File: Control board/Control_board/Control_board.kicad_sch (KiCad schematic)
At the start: 56 parts, among them J1 KEYPAD, J2 UART_conn, J3 Power_IN, J4 SPI_conn, SW1 RESET, U1 AT45DB321E-SHF-T, U10 SP3485EN, U2 LM2576HVS-5, U3 LoRa, U4 Wifi, U5 LM1117LD-3.3, U6 STM32F103C8Tx, U7 RTC_DS3234, U8 DS3232SN-T&R, U9 OLED, Y1 8MHZ

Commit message: edit layout
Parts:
- added D7: DF02S, Diode_SMD:Diode_Bridge_OnSemi_SDIP-4L, symbol Diode_Bridge:DF02S
- TH1, TH2: value Thermistor_PTC -> 250-120U
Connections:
- net 12V: now also D7.1 (+); no longer J3.1 (Pin_1)
- net GND: now also D7.2 (-); no longer J3.2 (Pin_2)
- new net: D7.3, J3.2 (Pin_2)
- new net: D7.4, J3.1 (Pin_1)
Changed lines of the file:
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@@
 	(wire
 		(pts
+			(xy 226.06 132.715) (xy 226.06 125.73)
+		)
+		(stroke
+			(width 0)
+			(type default)
+		)
+	)
+	(wire
+		(pts
 			(xy 205.105 29.21) (xy 205.105 34.29)
 		)
@@
 	(wire
 		(pts
-			(xy 234.95 135.255) (xy 240.03 135.255)
+			(xy 68.58 36.83) (xy 71.755 36.83)
 		)
 		(stroke
@@
 	(wire
 		(pts
-			(xy 68.58 36.83) (xy 71.755 36.83)
+			(xy 78.74 106.68) (xy 85.725 106.68)
 		)
 		(stroke
@@
 	(wire
 		(pts
-			(xy 78.74 106.68) (xy 85.725 106.68)
+			(xy 123.19 73.66) (xy 130.81 73.66)
 		)
 		(stroke
@@
 	(wire
 		(pts
-			(xy 123.19 73.66) (xy 130.81 73.66)
+			(xy 212.09 125.73) (xy 212.09 128.905)
 		)
 		(stroke
@@
 	(wire
 		(pts
+			(xy 226.06 135.255) (xy 226.06 144.145)
+		)
+		(stroke
+			(width 0)
+			(type default)
+		)
+	)
+	(wire
+		(pts
 			(xy 67.31 160.655) (xy 75.565 160.655)
 		)
@@
 	(wire
 		(pts
-			(xy 55.88 44.45) (xy 55.88 41.91)
+			(xy 219.71 136.525) (xy 221.615 136.525)
 		)
 		(stroke
@@
 	(wire
 		(pts
-			(xy 81.915 96.52) (xy 76.2 96.52)
+			(xy 55.88 44.45) (xy 55.88 41.91)
 		)
 		(stroke
@@
 	(wire
 		(pts
-			(xy 271.78 27.305) (xy 271.78 21.59)
+			(xy 81.915 96.52) (xy 76.2 96.52)
 		)
 		(stroke
@@
 	(wire
 		(pts
-			(xy 75.565 159.385) (xy 75.565 160.655)
+			(xy 271.78 27.305) (xy 271.78 21.59)
 		)
 		(stroke
@@
 	(wire
 		(pts
-			(xy 262.89 39.37) (xy 263.525 39.37)
+			(xy 75.565 159.385) (xy 75.565 160.655)
 		)
 		(stroke
@@
 	(wire
 		(pts
-			(xy 140.97 104.14) (xy 146.05 104.14)
+			(xy 262.89 39.37) (xy 263.525 39.37)
 		)
 		(stroke
@@
 	(wire
 		(pts
-			(xy 255.905 104.14) (xy 260.35 104.14)
+			(xy 140.97 104.14) (xy 146.05 104.14)
 		)
 		(stroke
@@
 	(wire
 		(pts
-			(xy 81.915 96.52) (xy 100.965 96.52)
+			(xy 255.905 104.14) (xy 260.35 104.14)
 		)
 		(stroke
@@
 	(wire
 		(pts
-			(xy 235.585 132.715) (xy 240.03 132.715)
+			(xy 81.915 96.52) (xy 100.965 96.52)
 		)
 		(stroke
@@
 	(wire
 		(pts
+			(xy 226.06 144.145) (xy 212.09 144.145)
+		)
+		(stroke
+			(width 0)
+			(type default)
+		)
+	)
+	(wire
+		(pts
 			(xy 207.01 105.41) (xy 219.075 105.41)
 		)
@@
 	(wire
 		(pts
+			(xy 226.06 135.255) (xy 240.03 135.255)
+		)
+		(stroke
+			(width 0)
+			(type default)
+		)
+	)
+	(wire
+		(pts
 			(xy 207.01 110.49) (xy 219.075 110.49)
 		)
@@
 	(wire
 		(pts
+			(xy 226.06 132.715) (xy 240.03 132.715)
+		)
+		(stroke
+			(width 0)
+			(type default)
+		)
+	)
+	(wire
+		(pts
 			(xy 167.64 35.56) (xy 163.83 35.56)
 		)
@@
 	(wire
 		(pts
+			(xy 201.93 136.525) (xy 204.47 136.525)
+		)
+		(stroke
+			(width 0)
+			(type default)
+		)
+	)
+	(wire
+		(pts
 			(xy 124.46 58.42) (xy 130.81 58.42)
 		)
@@
 	(wire
 		(pts
+			(xy 226.06 125.73) (xy 212.09 125.73)
+		)
+		(stroke
+			(width 0)
+			(type default)
+		)
+	)
+	(wire
+		(pts
 			(xy 106.68 136.525) (xy 106.68 139.7)
 		)
@@
 	)
 	(label "GND"
-		(at 234.95 135.255 0)
+		(at 201.93 136.525 0)
 		(effects
 			(font
@@
 	)
 	(label "12V"
-		(at 235.585 132.715 0)
+		(at 221.615 136.525 0)
 		(effects
 			(font
@@
 	)
 	(symbol
+		(lib_id "Diode_Bridge:DF02S")
+		(at 212.09 136.525 0)
+		(unit 1)
+		(exclude_from_sim no)
+		(in_bom yes)
+		(on_board yes)
+		(dnp no)
+		(fields_autoplaced yes)
+		(property "Reference" "D7"
+			(at 220.98 130.1048 0)
+			(effects
+				(font
+					(size 1.27 1.27)
+				)
+			)
+		)
+		(property "Value" "DF02S"
+			(at 220.98 132.6448 0)
+			(effects
+				(font
+					(size 1.27 1.27)
+				)
+			)
+		)
+		(property "Footprint" "Diode_SMD:Diode_Bridge_OnSemi_SDIP-4L"
+			(at 215.9 133.35 0)
+			(effects
+				(font
+					(size 1.27 1.27)
+				)
+				(justify left)
+				(hide yes)
+			)
+		)
+		(property "Datasheet" "https://www.onsemi.com/download/data-sheet/pdf/df10s-d.pdf"
+			(at 212.09 136.525 0)
+			(effects
+				(font
+					(size 1.27 1.27)
+				)
+				(hide yes)
+			)
+		)
+		(property "Description" "Bridge Rectifier, 140V Vrms, 1.5A If, SMDIP-4"
+			(at 212.09 136.525 0)
+			(effects
+				(font
+					(size 1.27 1.27)
+				)
+				(hide yes)
+			)
+		)
+		(pin "1"
+		)
+		(pin "3"
+		)
+		(pin "2"
+		)
+		(pin "4"
+		)
+		(instances
+			(project ""
+				(path "/6b6e7f04-e4bf-4c77-9852-1b9053859fbf"
+					(reference "D7")
+					(unit 1)
+				)
+			)
+		)
+	)
+	(symbol
 		(lib_id "Connector_Generic:Conn_01x08")
 		(at 269.875 138.43 0)
@@
 			)
 		)
-		(property "Value" "Thermistor_PTC"
+		(property "Value" "250-120U"
 			(at 85.09 135.255 90)
 			(effects
@@
 			)
 		)
-		(property "Value" "Thermistor_PTC"
+		(property "Value" "250-120U"
 			(at 86.36 144.78 90)
 			(effects

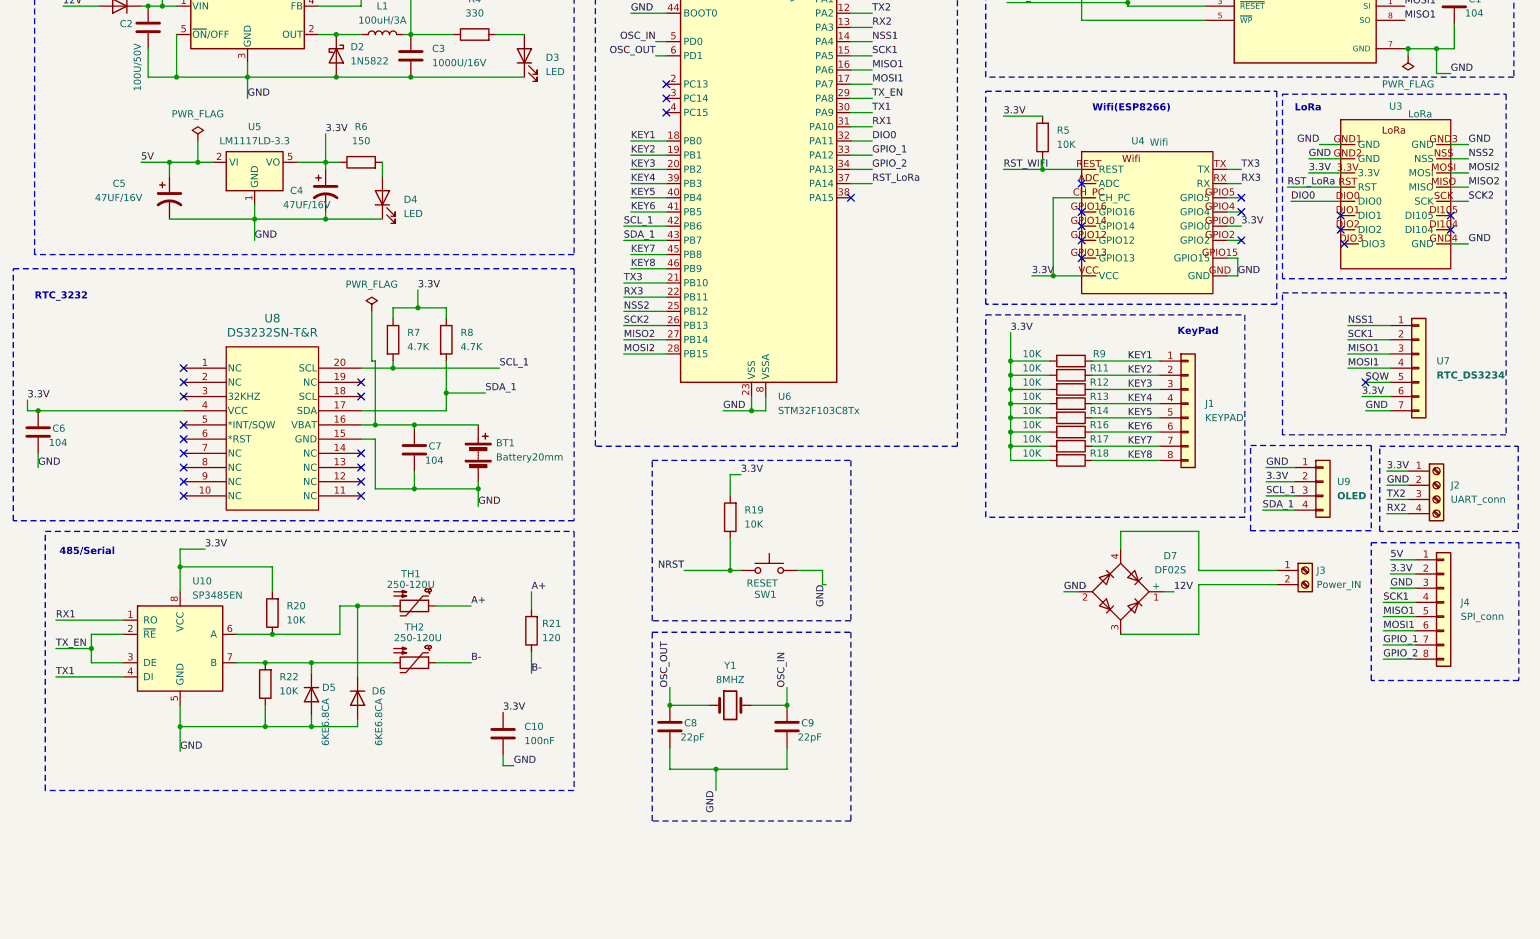
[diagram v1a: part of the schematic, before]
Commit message: Add ic to external GPIO
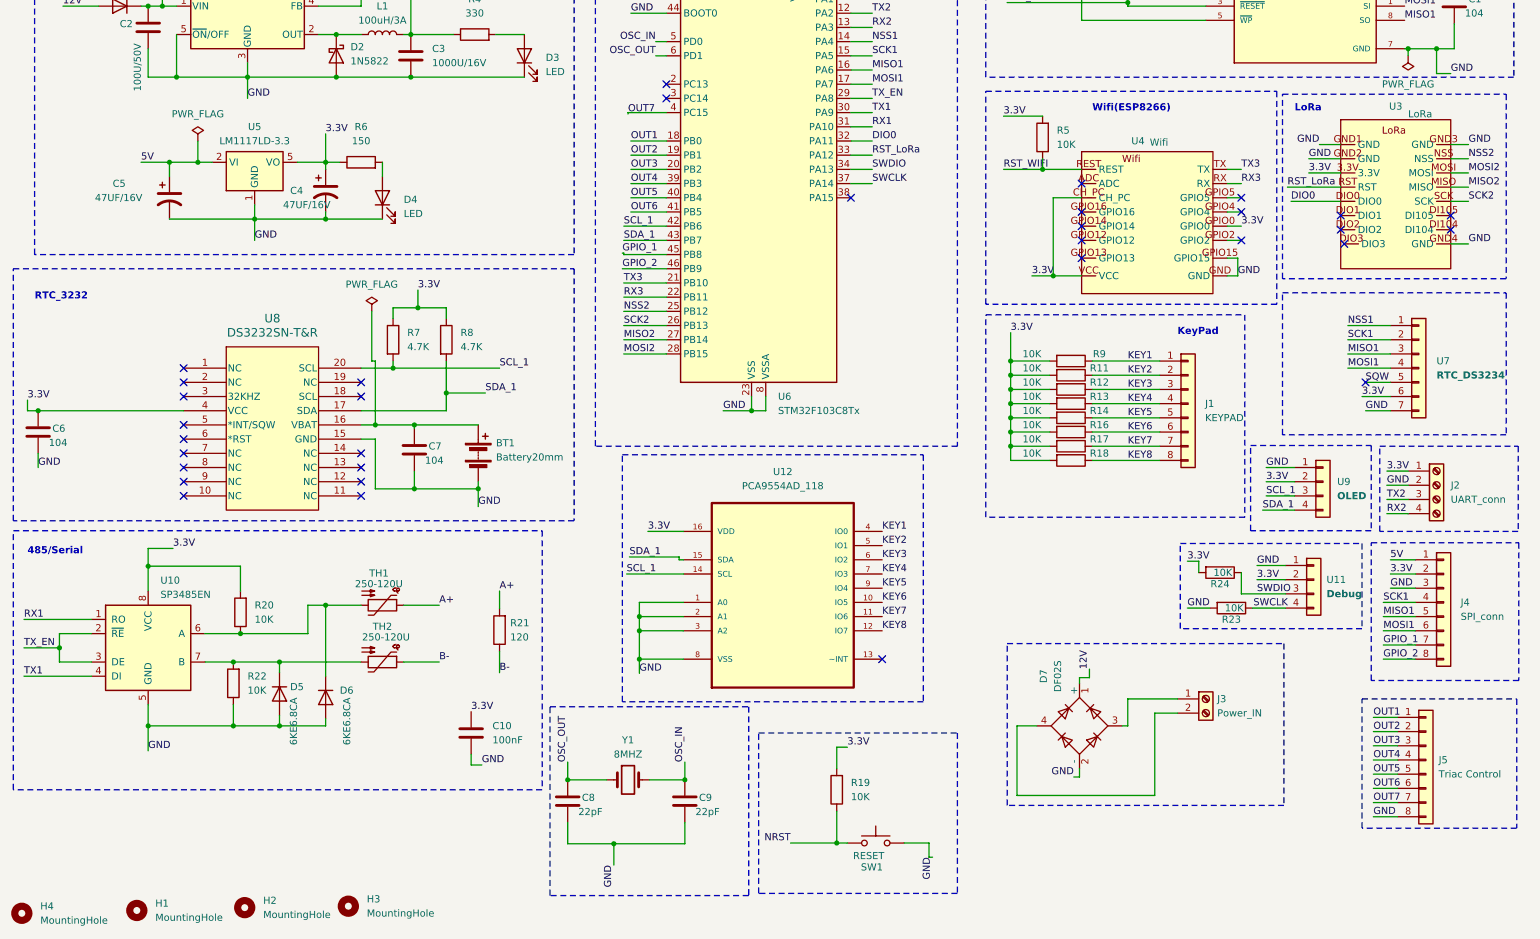
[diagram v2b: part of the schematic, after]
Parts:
- added H1, H2, H3, H4: MountingHole, MountingHole:MountingHole_3mm, symbol Mechanical:MountingHole
- added J5: Triac Control, smart_meter:RC8, symbol Connector_Generic:Conn_01x08
- added R23, R24: 10K, Resistor_SMD:R_1206_3216Metric, symbol Device:R
- added U11: Debug, Connector_PinSocket_2.54mm:PinSocket_1x04_P2.54mm_Vertical, symbol Connector_Generic:Conn_01x04
- added U12: PCA9554AD_118, smart_meter:SOIC127P1032X265-16N, symbol smart_meter:PCA9554AD_118
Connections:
- net 3.3V: now also R24.2, U11.2 (Pin_2), U12.16 (VDD)
- net GND: now also J5.8 (Pin_8), R23.2, U11.1 (Pin_1), U12.1 (A0), U12.2 (A1), U12.3 (A2), U12.8 (VSS)
- net GPIO_1: now also U6.45 (PB8); no longer U6.33 (PA12)
- net GPIO_2: now also U6.46 (PB9); no longer U6.34 (PA13)
- net KEY1: now also U12.4 (IO0); no longer U6.18 (PB0)
- net KEY2: now also U12.5 (IO1); no longer U6.19 (PB1)
- net KEY3: now also U12.6 (IO2); no longer U6.20 (PB2)
- net KEY4: now also U12.7 (IO3); no longer U6.39 (PB3)
- net KEY5: now also U12.9 (IO4); no longer U6.40 (PB4)
- net KEY6: now also U12.10 (IO5); no longer U6.41 (PB5)
- net KEY7: now also U12.11 (IO6); no longer U6.45 (PB8)
- net KEY8: now also U12.12 (IO7); no longer U6.46 (PB9)
- net RST_LoRa: now also U6.33 (PA12); no longer U6.37 (PA14)
- net SCL_1: now also U12.14 (SCL)
- net SDA_1: now also U12.15 (SDA)
- net at D7.3: now also J3.1 (Pin_1); no longer J3.2 (Pin_2)
- net at D7.4: now also J3.2 (Pin_2); no longer J3.1 (Pin_1)
- net OUT7: now reaches U6.4 (PC15)
- net OUT7: now also J5.7 (Pin_7)
- new net OUT1: J5.1 (Pin_1), U6.18 (PB0)
- new net OUT2: J5.2 (Pin_2), U6.19 (PB1)
- new net OUT3: J5.3 (Pin_3), U6.20 (PB2)
- new net OUT4: J5.4 (Pin_4), U6.39 (PB3)
- new net OUT5: J5.5 (Pin_5), U6.40 (PB4)
- new net OUT6: J5.6 (Pin_6), U6.41 (PB5)
- new net SWCLK: R23.1, U11.4 (Pin_4), U6.37 (PA14)
- new net SWDIO: R24.1, U11.3 (Pin_3), U6.34 (PA13)
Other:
- moved on the sheet: C10, C8, C9, D5, D6, D7, J3, R19, R20, R21, R22, SW1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

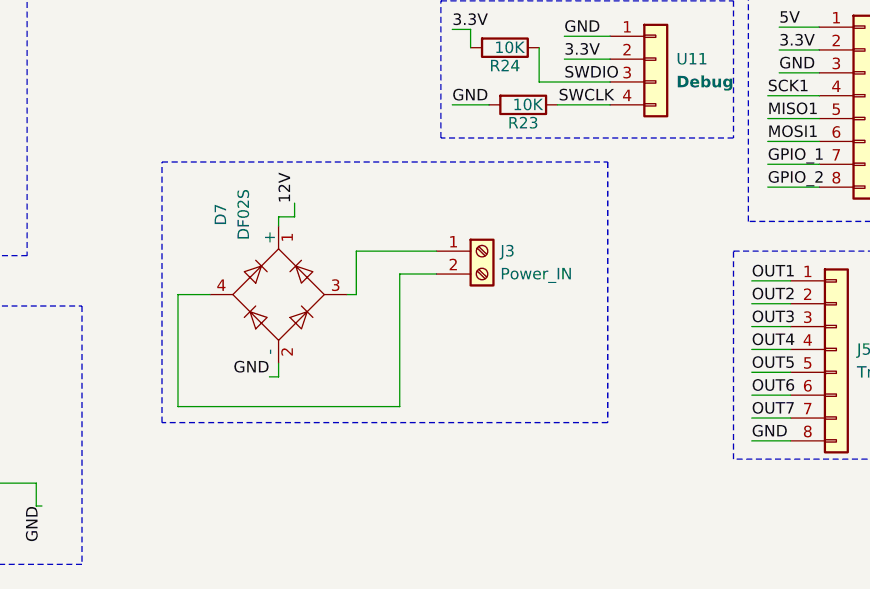
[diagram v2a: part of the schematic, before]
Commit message: Routing Power ctr
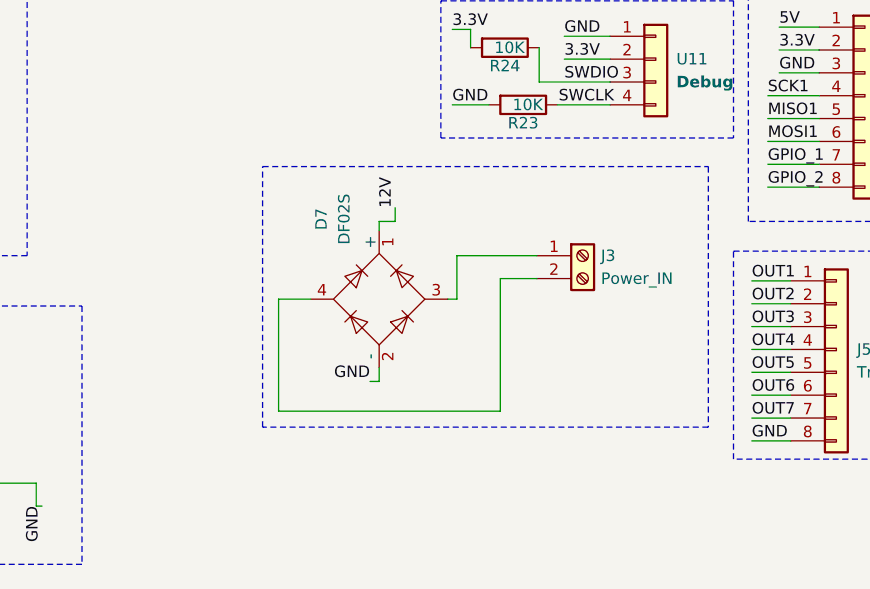
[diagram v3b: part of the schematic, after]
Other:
- moved on the sheet: D7, J3
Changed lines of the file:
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@@
 	(generator "eeschema")
 	(generator_version "9.0")
-	(paper "A4")
+	(paper "A3")
 	(rectangle
 		(start 122.936 112.014)
@@
 	)
 	(rectangle
-		(start 191.77 145.796)
-		(end 241.3 174.752)
+		(start 202.946 146.304)
+		(end 252.476 175.26)
 		(stroke
 			(width 0)
@@
 	(wire
 		(pts
-			(xy 206.502 151.892) (xy 204.724 151.892)
+			(xy 217.678 152.4) (xy 215.9 152.4)
 		)
 		(stroke
@@
 	(wire
 		(pts
-			(xy 204.724 151.892) (xy 204.724 152.908)
+			(xy 215.9 152.4) (xy 215.9 153.416)
 		)
 		(stroke
@@
 	(wire
 		(pts
-			(xy 213.36 160.528) (xy 213.36 155.702)
+			(xy 224.536 161.036) (xy 224.536 156.21)
 		)
 		(stroke
@@
 	(wire
 		(pts
-			(xy 193.548 160.528) (xy 197.104 160.528)
+			(xy 204.724 161.036) (xy 208.28 161.036)
 		)
 		(stroke
@@
 	(wire
 		(pts
-			(xy 218.186 158.242) (xy 218.186 172.974)
+			(xy 229.362 158.75) (xy 229.362 173.482)
 		)
 		(stroke
@@
 	(wire
 		(pts
-			(xy 212.344 160.528) (xy 213.36 160.528)
+			(xy 223.52 161.036) (xy 224.536 161.036)
 		)
 		(stroke
@@
 	(wire
 		(pts
-			(xy 203.708 169.672) (xy 204.724 169.672)
+			(xy 214.884 170.18) (xy 215.9 170.18)
 		)
 		(stroke
@@
 	(wire
 		(pts
-			(xy 204.724 168.148) (xy 204.724 169.672)
+			(xy 215.9 168.656) (xy 215.9 170.18)
 		)
 		(stroke
@@
 	(wire
 		(pts
-			(xy 222.25 158.242) (xy 218.186 158.242)
+			(xy 233.426 158.75) (xy 229.362 158.75)
 		)
 		(stroke
@@
 	(wire
 		(pts
-			(xy 218.186 172.974) (xy 193.548 172.974)
+			(xy 229.362 173.482) (xy 204.724 173.482)
 		)
 		(stroke
@@
 	(wire
 		(pts
-			(xy 193.548 172.974) (xy 193.548 160.528)
+			(xy 204.724 173.482) (xy 204.724 161.036)
 		)
 		(stroke
@@
 	(wire
 		(pts
-			(xy 213.36 155.702) (xy 222.25 155.702)
+			(xy 224.536 156.21) (xy 233.426 156.21)
 		)
 		(stroke
@@
 	(wire
 		(pts
-			(xy 206.502 150.368) (xy 206.502 151.892)
+			(xy 217.678 150.876) (xy 217.678 152.4)
 		)
 		(stroke
@@
 	)
 	(label "GND"
-		(at 203.708 169.672 180)
+		(at 214.884 170.18 180)
 		(effects
 			(font
@@
 	)
 	(label "12V"
-		(at 206.502 150.368 90)
+		(at 217.678 150.876 90)
 		(effects
 			(font
@@
 	(symbol
 		(lib_id "Diode_Bridge:DF02S")
-		(at 204.724 160.528 90)
+		(at 215.9 161.036 90)
 		(unit 1)
 		(exclude_from_sim no)
@@
 		(fields_autoplaced yes)
 		(property "Reference" "D7"
-			(at 198.3038 151.638 0)
+			(at 209.4798 152.146 0)
 			(effects
 				(font
@@
 		)
 		(property "Value" "DF02S"
-			(at 200.8438 151.638 0)
+			(at 212.0198 152.146 0)
 			(effects
 				(font
@@
 		)
 		(property "Footprint" "Diode_SMD:Diode_Bridge_OnSemi_SDIP-4L"
-			(at 201.549 156.718 0)
+			(at 212.725 157.226 0)
 			(effects
 				(font
@@
 		)
 		(property "Datasheet" "https://www.onsemi.com/download/data-sheet/pdf/df10s-d.pdf"
-			(at 204.724 160.528 0)
+			(at 215.9 161.036 0)
 			(effects
 				(font
@@
 		)
 		(property "Description" "Bridge Rectifier, 140V Vrms, 1.5A If, SMDIP-4"
-			(at 204.724 160.528 0)
+			(at 215.9 161.036 0)
 			(effects
 				(font
@@
 	(symbol
 		(lib_id "Connector:Screw_Terminal_01x02")
-		(at 227.33 155.702 0)
+		(at 238.506 156.21 0)
 		(unit 1)
 		(exclude_from_sim no)
@@
 		(fields_autoplaced yes)
 		(property "Reference" "J3"
-			(at 229.362 155.7019 0)
+			(at 240.538 156.2099 0)
 			(effects
 				(font
@@
 		)
 		(property "Value" "Power_IN"
-			(at 229.362 158.2419 0)
+			(at 240.538 158.7499 0)
 			(effects
 				(font
@@
 		)
 		(property "Footprint" "smart_meter:RC2"
-			(at 227.33 155.702 0)
+			(at 238.506 156.21 0)
 			(effects
 				(font
@@
 		)
 		(property "Datasheet" "~"
-			(at 227.33 155.702 0)
+			(at 238.506 156.21 0)
 			(effects
 				(font
@@
 		)
 		(property "Description" "Generic screw terminal, single row, 01x02, script generated (kicad-library-utils/schlib/autogen/connector/)"
-			(at 227.33 155.702 0)
+			(at 238.506 156.21 0)
 			(effects
 				(font

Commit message: Routing control board
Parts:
- removed U5: LM1117LD-3.3, Package_SON:WSON-8-1EP_4x4mm_P0.8mm_EP2.2x3mm, symbol Regulator_Linear:LM1117LD-3.3
- added JP1: TX1_selector, Connector_PinHeader_2.54mm:PinHeader_1x03_P2.54mm_Vertical, symbol Jumper:Jumper_3_Open
- added JP2: RX1_Selector, Connector_PinHeader_2.54mm:PinHeader_1x03_P2.54mm_Vertical, symbol Jumper:Jumper_3_Open
- added R25, R26: 10K, Resistor_SMD:R_1206_3216Metric, symbol Device:R
- added SW2: Button1, Button_Switch_SMD:SW_Tactile_SPST_NO_Straight_CK_PTS636Sx25SMTRLFS, symbol Switch:SW_Push
- added SW3: Button2, Button_Switch_SMD:SW_Tactile_SPST_NO_Straight_CK_PTS636Sx25SMTRLFS, symbol Switch:SW_Push
- added U13: LM317DCY, smart_meter:LM3.3V, symbol smart_meter:LM317DCY
- J2: footprint Connector_PinHeader_2.54mm:PinHeader_1x04_P2.54mm_Vertical -> smart_meter:RC4
- J4: footprint Connector_PinSocket_2.54mm:PinSocket_1x08_P2.54mm_Vertical -> smart_meter:RC8
- U12: footprint smart_meter:SOIC127P1032X265-16N -> smart_meter:PCA955
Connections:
- net 3.3V: now also R25.2, R26.2, U13.2 (OUTPUT), U13.4 (OUTPUT)
- net 5V: now also U13.3 (INPUT)
- net GND: now also SW2.2, SW3.2, U13.1 (ADJUST)
- net RX1: now also JP2.2 (C); no longer U10.1 (RO)
- net TX1: now also JP1.2 (C); no longer U10.4 (DI)
- net Button1: now reaches U6.2 (PC13)
- net Button1: now also R25.1, SW2.1
- net Button2: now reaches U6.3 (PC14)
- net Button2: now also R26.1, SW3.1
- new net RX_485: JP2.3 (B), U10.1 (RO)
- new net RX_MDB: JP2.1 (A)
- new net TX_485: JP1.3 (B), U10.4 (DI)
- new net TX_MDB: JP1.1 (A)
- no-connect marks 34 -> 32
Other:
- added sheet MDB_uart (MDB_uart.kicad_sch)
- moved on the sheet: C4, D4, H1, H2, H3, H4, R6
